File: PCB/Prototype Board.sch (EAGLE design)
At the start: 30 parts, among them Q3 20V/4.2A/52mΩ/1.4W, U1 9DoF IMU, U3 ESP-WROOM-32, U5 DWM1000, U6 1.8V/100mA, U7 CH340C, U8 XC6222B331MR-G

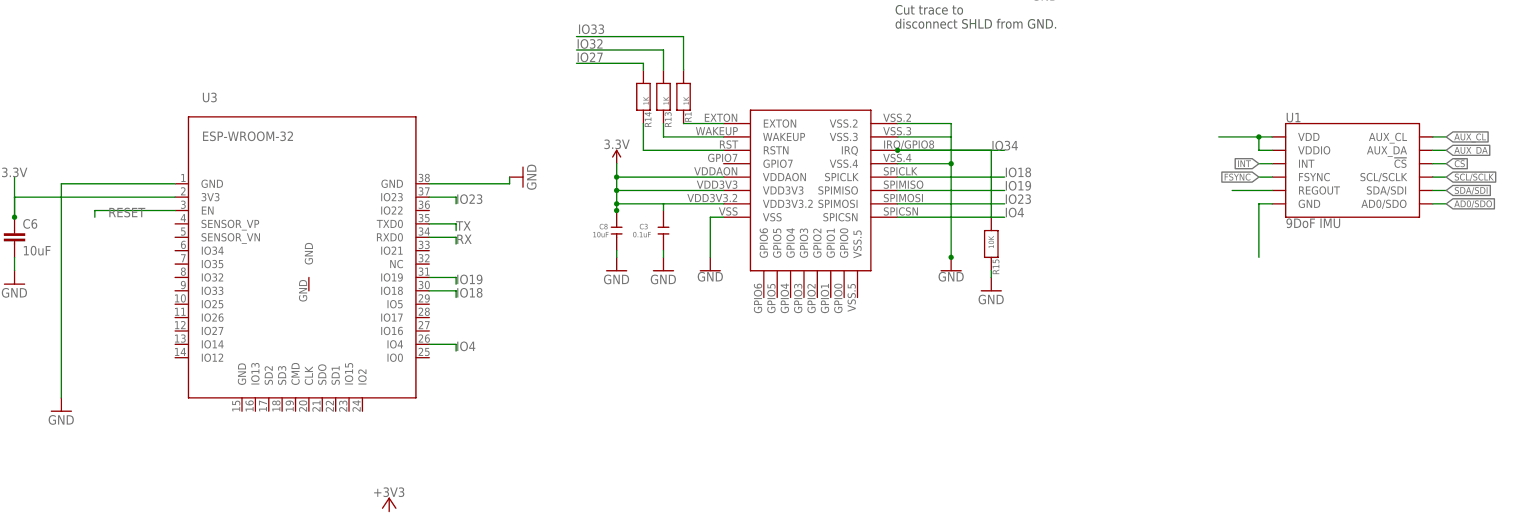
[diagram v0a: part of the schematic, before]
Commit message: Partially connected the IMU unit to the ESP32
Might need level shifting, haven't tied all the pins yet
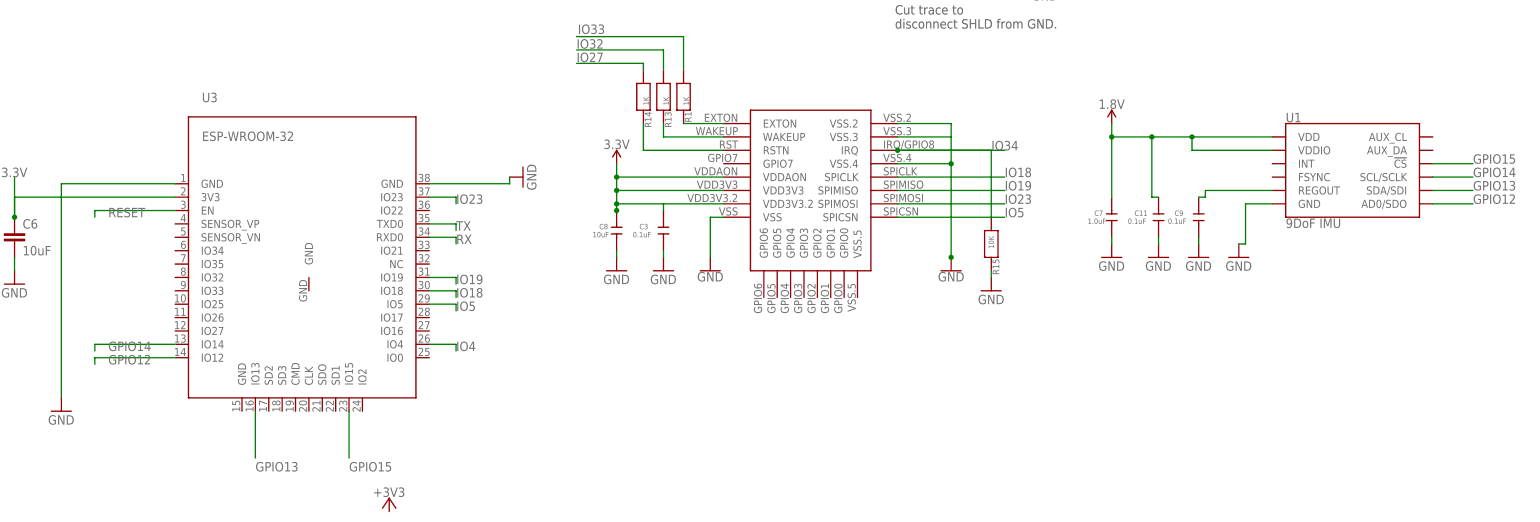
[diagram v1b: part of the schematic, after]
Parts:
- added C11, C9: 0.1uF, Discrete:C-0603
- added C7: 1.0uF, Discrete:C-0603
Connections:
- removed net !CS: U1.!CS
- removed net AD0/SDO: U1.AD0/SDO
- removed net AUX_CL: U1.AUX_CL
- removed net AUX_DA: U1.AUX_DA
- removed net FSYNC: U1.FSYNC
- removed net GND1: U1.GND
- removed net INT: U1.INT
- removed net N$1: U1.REGOUT
- removed net SCL/SCLK: U1.SCL/SCLK
- removed net SDA/SDI: U1.SDA/SDI
- new net GPIO12: U1.AD0/SDO, U3.IO12
- new net GPIO13: U1.SDA/SDI, U3.IO13
- new net GPIO14: U1.SCL/SCLK, U3.IO14
- new net GPIO15: U1.!CS, U3.IO15
- new net IO5: U3.IO5, U5.SPICSN
- new net N$13: C9.1, U1.REGOUT
- net 1.8V: now also C11.1, C7.1
- net GND: now also C11.2, C7.2, C9.2, U1.GND
- net IO4: no longer U5.SPICSN

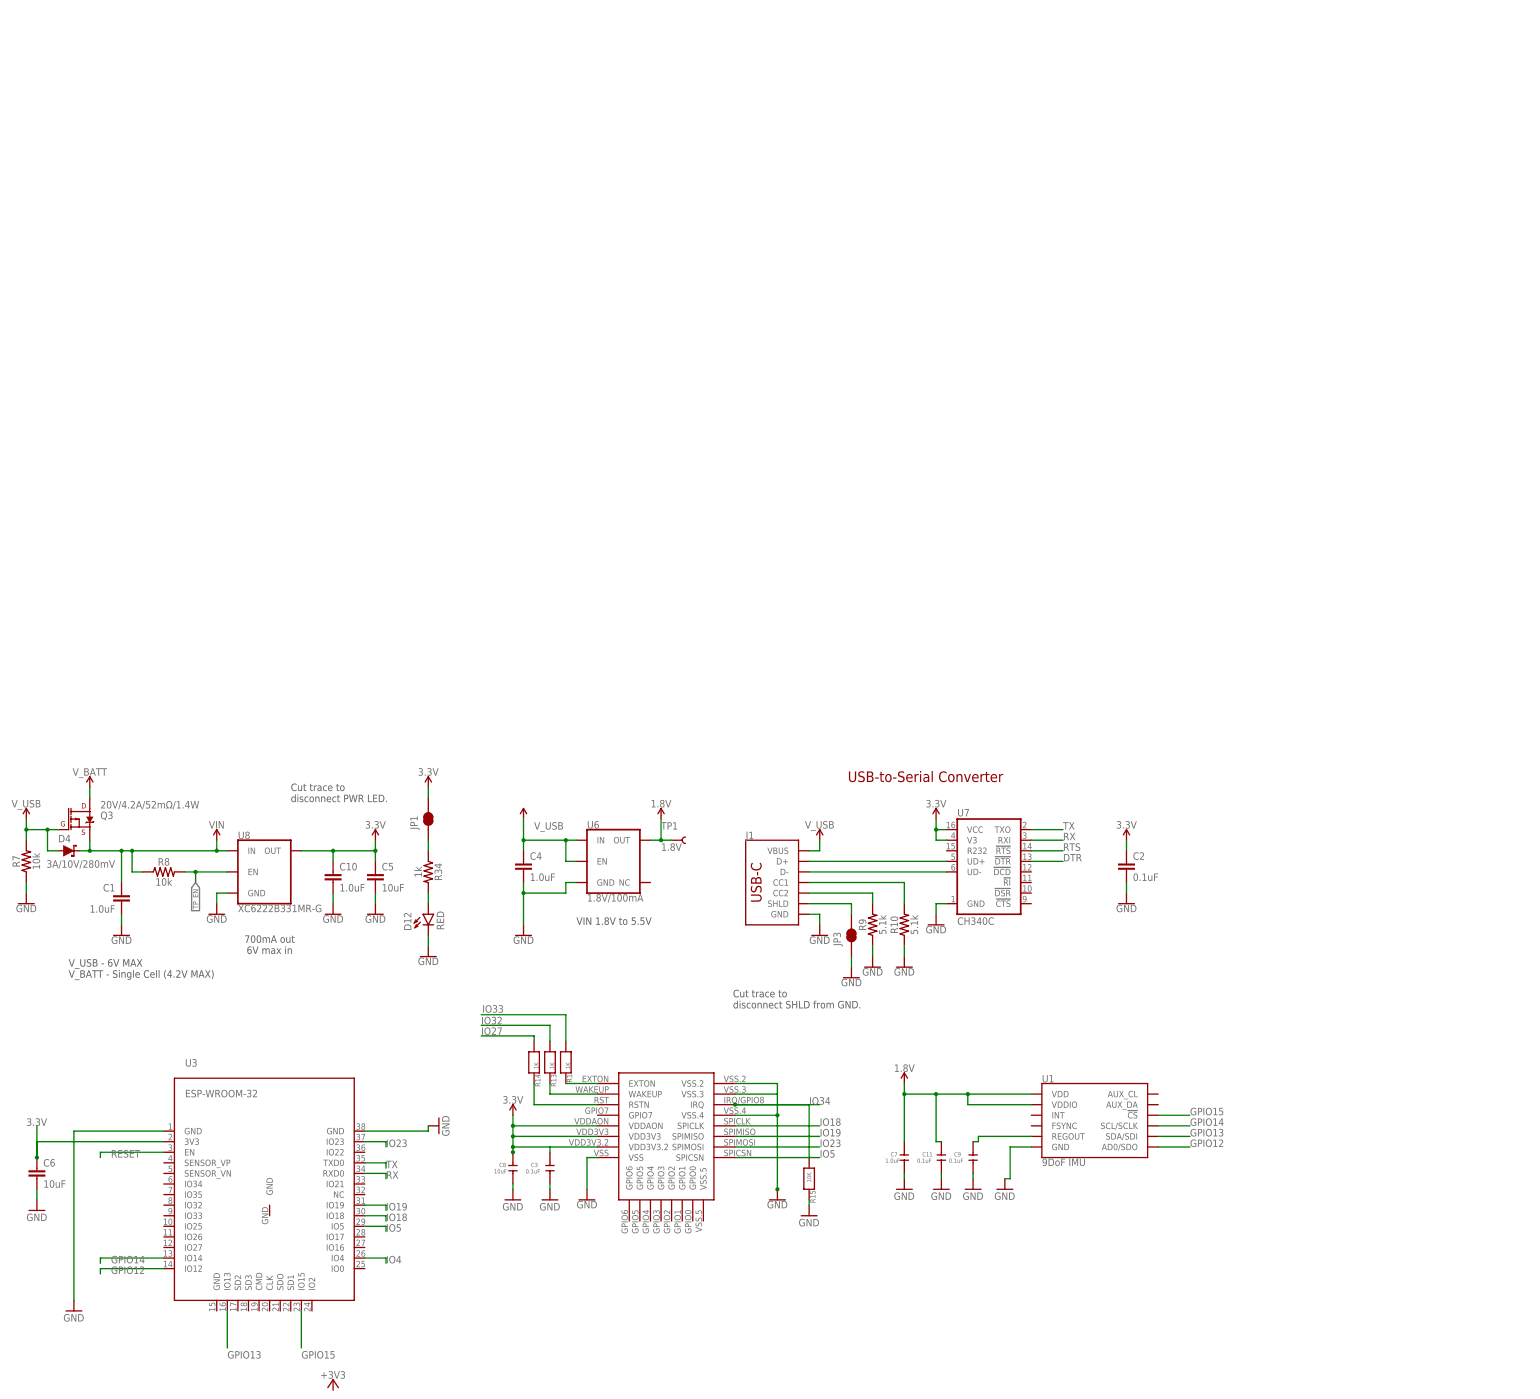
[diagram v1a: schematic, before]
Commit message: Added Level Shifting, Updated Power Supply, Finished Connecting Components
The core schematic is almost done, may need some additional touches for optional functionality. Once this is done, we can proceed to route all the connections (e.g. commit to the board file)
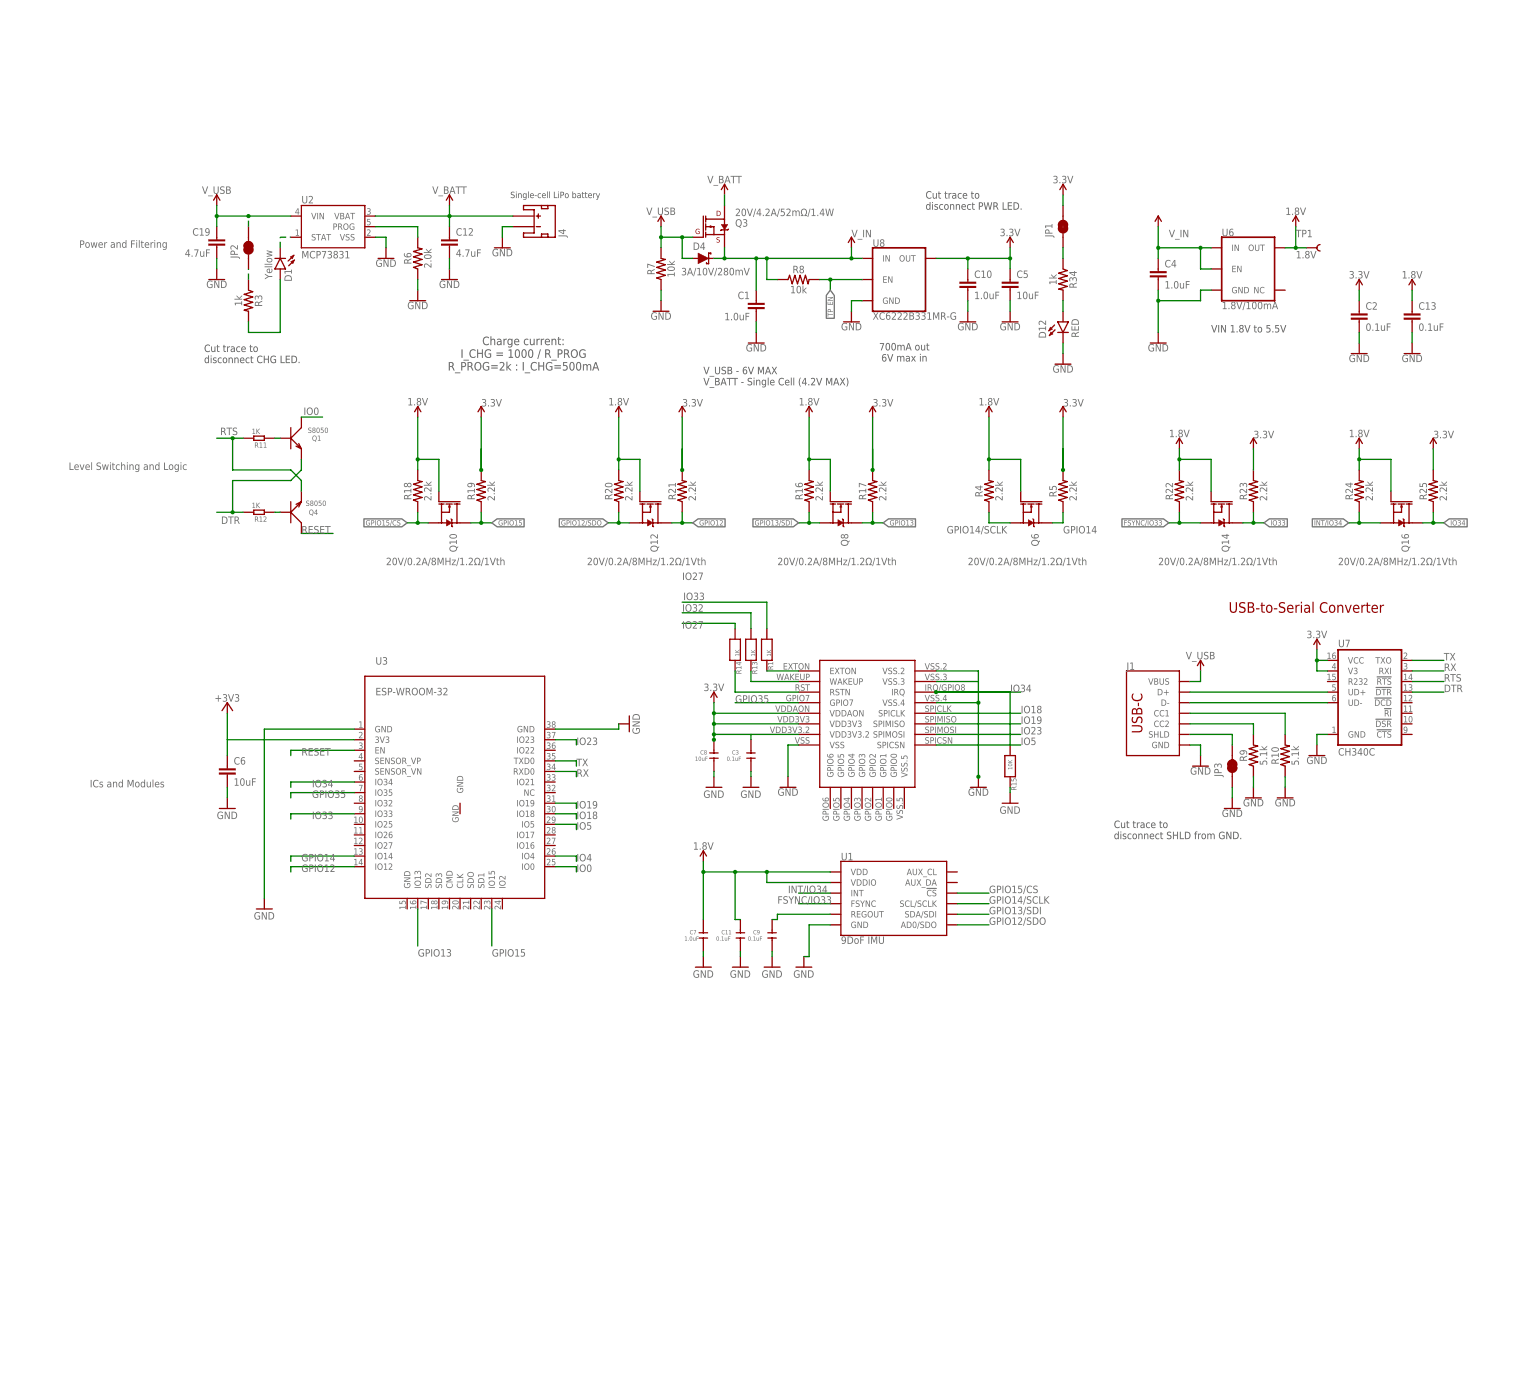
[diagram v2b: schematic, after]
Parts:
- added C12: 4.7uF, SparkFun-Capacitors:4.7UF-0402_TIGHT-6.3V-20%-X5R
- added C13: 0.1uF, SparkFun-Capacitors:0.1UF-0402T-6.3V-10%-X7R
- added C19: 4.7uF, SparkFun-Capacitors:4.7UF-0603-35V-(20%)
- added D1: Yellow, SparkFun-LED:LED-YELLOW0603
- added J4: (no value), SparkFun-Connectors:JST_2MM_MALE
- added JP2: JUMPER-SMT_2_NC_TRACE_SILK, SparkFun-Jumpers:JUMPER-SMT_2_NC_TRACE_SILK
- added Q1, Q4: S8050, Discrete:TRANSISTOR-NPN-SOT23
- added Q10, Q12, Q14, Q16, Q6, Q8: 20V/0.2A/8MHz/1.2Ω/1Vth, SparkFun-DiscreteSemi:MOSFET-NCH-RE1C002UN
- added R11, R12: 1K, Discrete:R-0603
- added R16, R17, R18, R19, R20, R21, R22, R23, R24, R25, R4, R5: 2.2k, SparkFun-Resistors:2.2KOHM-0402T-1/16W-1%
- added R3: 1k, SparkFun-Resistors:1KOHM-0402T-1/16W-1%
- added R6: 2.0k, SparkFun-Resistors:2.0KOHM-0603-1/10W-5%
- added U2: MCP73831, SparkFun-IC-Power:MCP73831
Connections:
- removed net VIN: C1.1, D4.C, Q3.S, R8.1, U8.IN
- new net +3V3: C6.1, U3.3V3
- new net CHG_LED: D1.A, R3.2
- new net FSYNC/IO33: Q14.S, R22.1, U1.FSYNC
- new net GPIO12/SDO: Q12.S, R20.1, U1.AD0/SDO
- new net GPIO13/SDI: Q8.S, R16.1, U1.SDA/SDI
- new net GPIO14/SCLK: Q6.S, R4.1, U1.SCL/SCLK
- new net GPIO15/CS: Q10.S, R18.1, U1.!CS
- new net GPIO35: U3.IO35, U5.GPIO7
- new net INT/IO34: Q16.S, R24.1, U1.INT
- new net IO0: Q1.C, U3.IO0
- new net N$1: Q4.B, R12.1
- new net N$14: Q1.B, R11.1
- new net N$3: R6.2, U2.PROG
- new net N$4: JP2.1, R3.1
- new net N$7: D1.C, U2.STAT
- new net V_IN: C1.1, C4.1, D4.C, Q3.S, R8.1, U6.EN, U6.IN, U8.IN
- net 1.8V: now also C13.1, Q10.G, Q12.G, Q14.G, Q16.G, Q6.G, Q8.G, R16.2, R18.2, R20.2, R22.2, R24.2, R4.2
- net 3.3V: now also R17.2, R19.2, R21.2, R23.2, R25.2, R5.2; no longer C6.1, U3.3V3
- net DTR: now also Q1.E, R12.2
- net GND: now also C12.2, C13.2, C19.2, J4.-, R6.1, U2.VSS
- net GPIO12: now also Q12.D, R21.1; no longer U1.AD0/SDO
- net GPIO13: now also Q8.D, R17.1; no longer U1.SDA/SDI
- net GPIO14: now also Q6.D, R5.1; no longer U1.SCL/SCLK
- net GPIO15: now also Q10.D, R19.1; no longer U1.!CS
- net IO33: now also Q14.D, R23.1, U3.IO33
- net IO34: now also Q16.D, R25.1, U3.IO34
- net RESET: now also Q4.C
- net RTS: now also Q4.E, R11.2
- net V_BATT: now also C12.1, J4.+, U2.VBAT
- net V_USB: now also C19.1, JP2.2, U2.VIN; no longer C4.1, U6.EN, U6.IN
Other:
- note added: "Charge current: I_CHG = 1000 / R_PROG R_PROG=2k : I_CHG=500mA"
- note added: "Cut trace to disconnect CHG LED."
- note added: "ICs and Modules"
- note added: "Level Switching and Logic"
- note added: "Power and Filtering"
- note added: "Single-cell LiPo battery"
- moved on the sheet: C1, C10, C11, C2, C3, C4, C5, C6, C7, C8, C9, D12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

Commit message: Began laying out components on the board
We're going to need a 4 layered board and fine trace control, which means we'll probably have to order from JCBPCL rather than use the FEDC fabs.
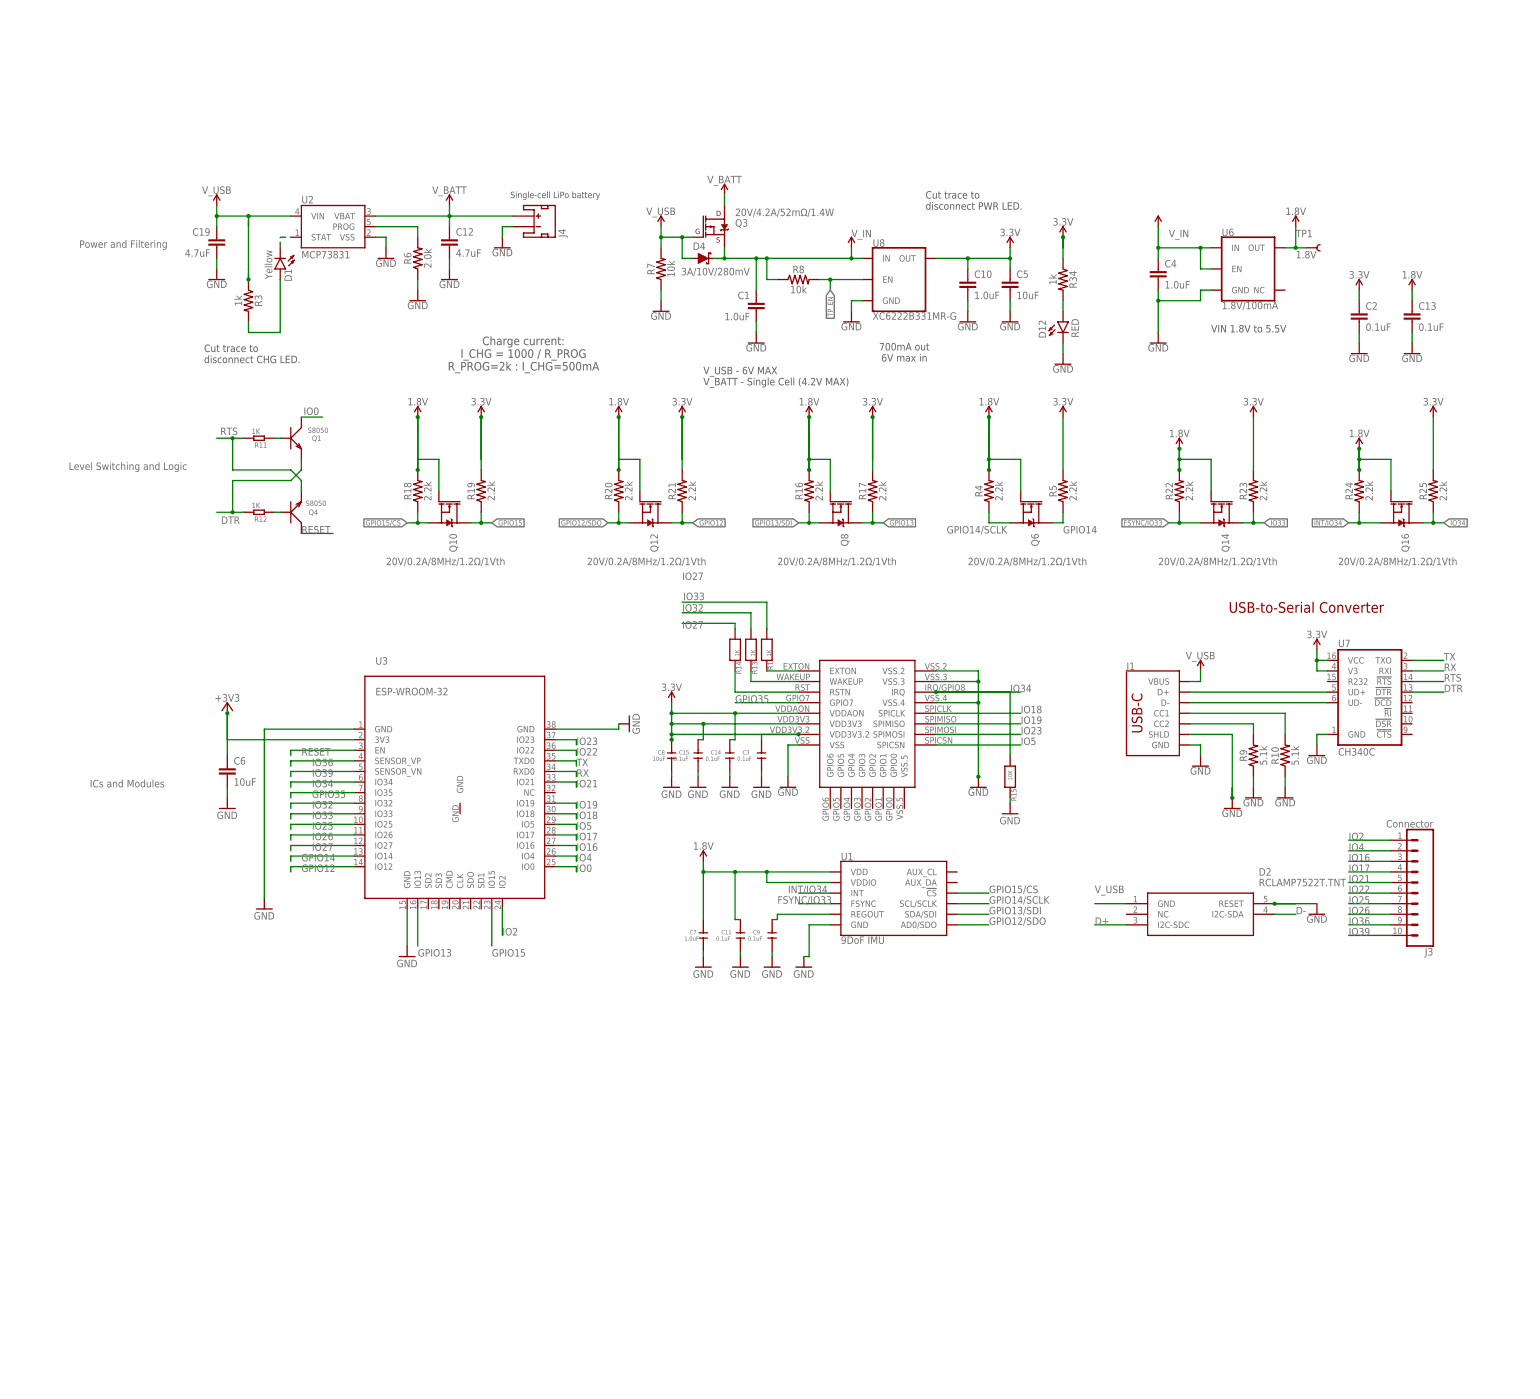
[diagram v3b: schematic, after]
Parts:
- removed JP1, JP2, JP3: JUMPER-SMT_2_NC_TRACE_SILK, SparkFun-Jumpers:JUMPER-SMT_2_NC_TRACE_SILK
- added C14, C15: 0.1uF, Discrete:C-0603
- added D2: RCLAMP7522T.TNT, RCLAMP7522T.TNT:RCLAMP7522T.TNT
- added J3: Connector, SparkFun-Connectors:CONN_10"
- C1, C10: device SparkFun-Capacitors:1.0UF-0402T-16V-10% -> SparkFun-Capacitors:1.0UF-0402-16V-10%
- C12: device SparkFun-Capacitors:4.7UF-0402_TIGHT-6.3V-20%-X5R -> SparkFun-Capacitors:4.7UF-1206-16V-(+80/-20%)
- C13, C2: device SparkFun-Capacitors:0.1UF-0402T-6.3V-10%-X7R -> SparkFun-Capacitors:0.1UF-0402-16V-10%
- C19: device SparkFun-Capacitors:4.7UF-0603-35V-(20%) -> SparkFun-Capacitors:4.7UF-1206-16V-(+80/-20%)
- C4: device SparkFun-Capacitors:1.0UF-0603-16V-10%-X7R -> SparkFun-Capacitors:1.0UF-0402-16V-10%
- C5: device SparkFun-Capacitors:10UF-0402T-6.3V-20% -> SparkFun-Capacitors:10UF-0603-6.3V-20%
- J1: value (none) -> USB Type C
- J4: value (none) -> Battery Connector
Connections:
- removed net N$4: JP2.1, R3.1
- removed net N$8: J1.SHLD, JP3.2
- new net IO16: J3.3, U3.IO16
- new net IO17: J3.4, U3.IO17
- new net IO2: J3.1, U3.IO2
- new net IO21: J3.5, U3.IO21
- new net IO22: J3.6, U3.IO22
- new net IO25: J3.7, U3.IO25
- new net IO26: J3.8, U3.IO26
- new net IO36: J3.9, U3.SENSOR_VP
- new net IO39: J3.10, U3.SENSOR_VN
- net 1.8V: no longer Q12.G, R20.2
- net 3.3V: now also C14.1, C15.1, R34.1; no longer JP1.2
- net D+: now also D2.I2C-SDC
- net D-: now also D2.I2C-SDA
- net GND: now also C14.2, C15.2, D2.RESET, J1.SHLD, U3.GND@15; no longer JP3.1
- net IO27: now also U3.IO27
- net IO32: now also U3.IO32
- net IO4: now also J3.2
- net N$2: now also Q12.G, R20.2; no longer JP1.1, R34.1
- net V_USB: now also D2.GND, R3.1; no longer JP2.2
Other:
- note removed: "Cut trace to disconnect SHLD from GND."
- moved on the sheet: C3, C8, R15
